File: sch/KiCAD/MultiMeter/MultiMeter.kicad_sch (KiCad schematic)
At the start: 17 parts

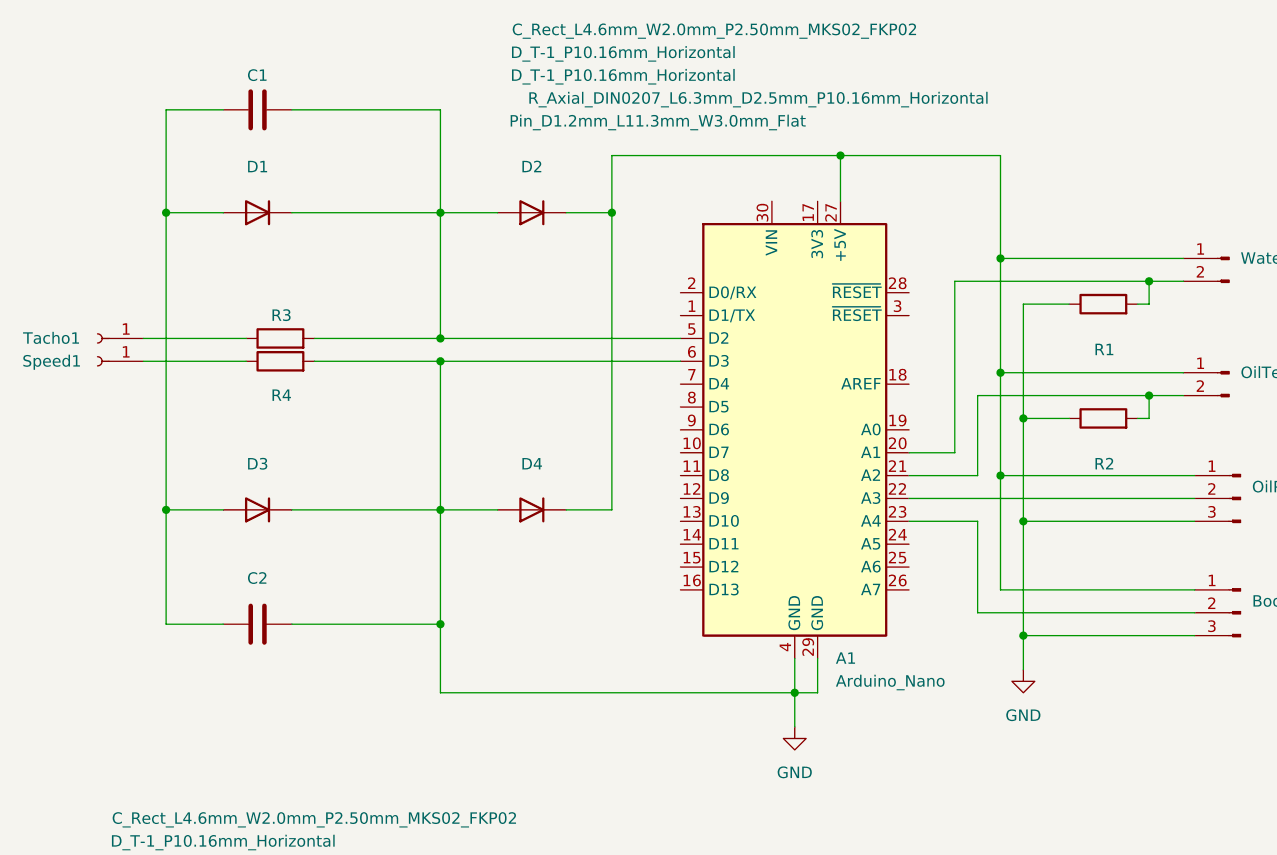
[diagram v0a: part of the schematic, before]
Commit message: 回路図の間違いを修正
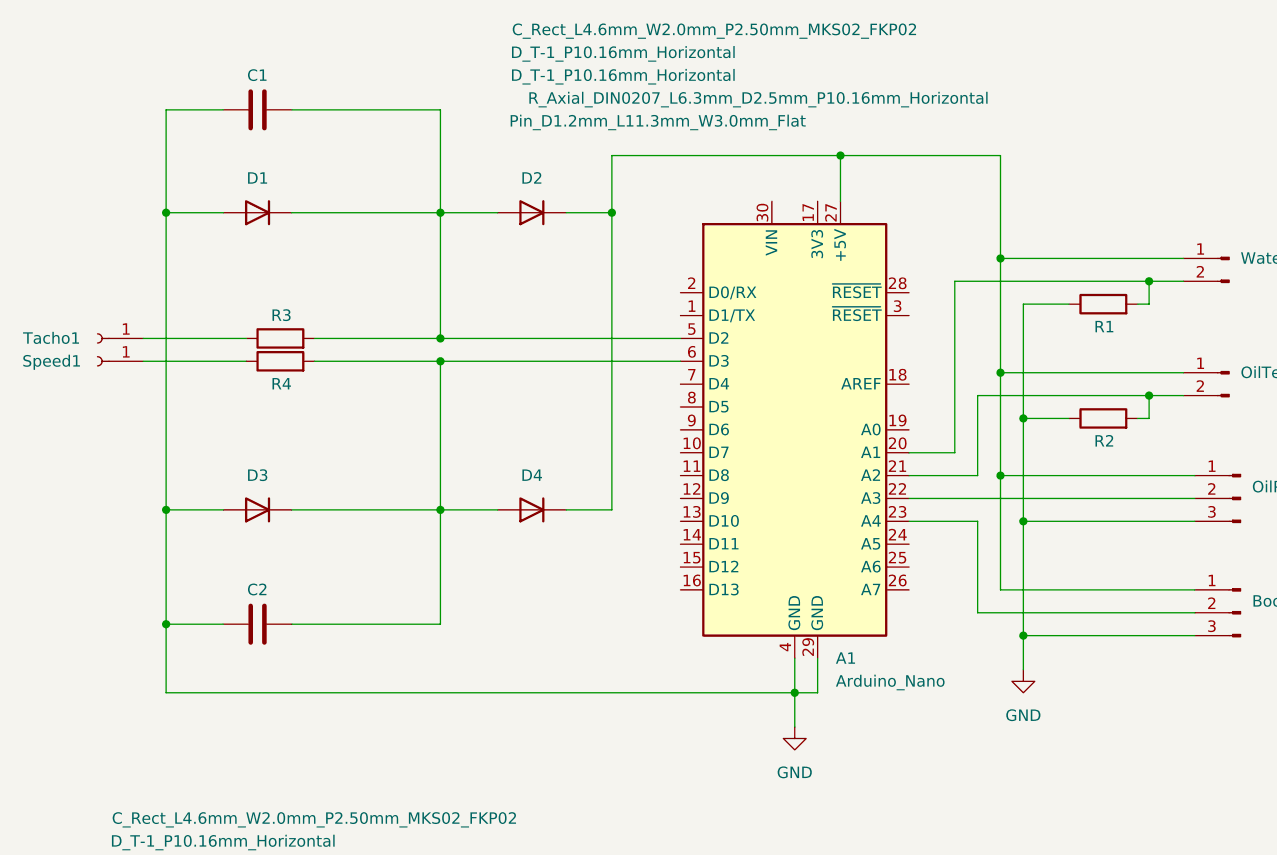
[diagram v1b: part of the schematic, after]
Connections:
- net GND: now also C1.1, C2.1, D1.1 (A), D3.1 (A); no longer A1.6 (D3), C2.2, D3.2 (K), D4.1 (A), R4.2
- new net: A1.6 (D3), C2.2, D3.2 (K), D4.1 (A), R4.2
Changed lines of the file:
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@@
 (kicad_sch (version 20211123) (generator eeschema)
   (paper "A4")
-  (junction (at 62.23 80.01) (diameter 0) (color 0 0 0 0)
-  )
   (junction (at 127 68.58) (diameter 0) (color 0 0 0 0)
   )
@@
   (junction (at 124.46 63.5) (diameter 0) (color 0 0 0 0)
   )
+  (junction (at 31.75 80.01) (diameter 0) (color 0 0 0 0)
+  )
   (junction (at 62.23 34.29) (diameter 0) (color 0 0 0 0)
   )
@@
     (stroke (width 0) (type default) (color 0 0 0 0))
   )
-  (wire (pts (xy 101.6 87.63) (xy 62.23 87.63))
-    (stroke (width 0) (type default) (color 0 0 0 0))
-  )
   (wire (pts (xy 119.38 60.96) (xy 114.3 60.96))
     (stroke (width 0) (type default) (color 0 0 0 0))
@@
     (stroke (width 0) (type default) (color 0 0 0 0))
   )
+  (wire (pts (xy 31.75 87.63) (xy 31.75 80.01))
+    (stroke (width 0) (type default) (color 0 0 0 0))
+  )
   (wire (pts (xy 81.28 34.29) (xy 76.2 34.29))
     (stroke (width 0) (type default) (color 0 0 0 0))
@@
     (stroke (width 0) (type default) (color 0 0 0 0))
   )
-  (wire (pts (xy 62.23 87.63) (xy 62.23 80.01))
-    (stroke (width 0) (type default) (color 0 0 0 0))
-  )
   (wire (pts (xy 144.78 41.91) (xy 140.97 41.91))
     (stroke (width 0) (type default) (color 0 0 0 0))
@@
     (stroke (width 0) (type default) (color 0 0 0 0))
   )
+  (wire (pts (xy 101.6 87.63) (xy 31.75 87.63))
+    (stroke (width 0) (type default) (color 0 0 0 0))
+  )
   (wire (pts (xy 139.7 57.15) (xy 140.97 57.15))
     (stroke (width 0) (type default) (color 0 0 0 0))
@@
   (symbol (lib_id "Device:R") (at 135.89 57.15 90) (unit 1)
     (in_bom yes) (on_board yes)
-    (property "Reference" "R2" (id 0) (at 137.16 62.23 90)
+    (property "Reference" "R2" (id 0) (at 137.16 59.69 90)
       (effects (font (size 1.27 1.27)) (justify left))
     )
@@
   (symbol (lib_id "Simulation_SPICE:DIODE") (at 41.91 67.31 0) (unit 1)
     (in_bom yes) (on_board yes)
-    (property "Reference" "D3" (id 0) (at 41.91 62.23 0))
+    (property "Reference" "D3" (id 0) (at 41.91 63.5 0))
     (property "Value" "D_T-1_P10.16mm_Horizontal" (id 1) (at 38.1 104.14 0))
     (property "Footprint" "Diode_THT:D_T-1_P10.16mm_Horizontal" (id 2) (at 41.91 67.31 0)
@@
   (symbol (lib_id "Device:R") (at 44.45 50.8 90) (unit 1)
     (in_bom yes) (on_board yes)
-    (property "Reference" "R4" (id 0) (at 45.72 54.61 90)
+    (property "Reference" "R4" (id 0) (at 45.72 53.34 90)
       (effects (font (size 1.27 1.27)) (justify left))
     )
@@
   (symbol (lib_id "Device:C") (at 41.91 80.01 90) (unit 1)
     (in_bom yes) (on_board yes)
-    (property "Reference" "C2" (id 0) (at 41.91 74.93 90))
+    (property "Reference" "C2" (id 0) (at 41.91 76.2 90))
     (property "Value" "C_Rect_L4.6mm_W2.0mm_P2.50mm_MKS02_FKP02" (id 1) (at 48.26 101.6 90))
     (property "Footprint" "Capacitor_THT:C_Rect_L4.6mm_W2.0mm_P2.50mm_MKS02_FKP02" (id 2) (at 45.72 79.0448 0)
@@
   (symbol (lib_id "Simulation_SPICE:DIODE") (at 72.39 34.29 0) (unit 1)
     (in_bom yes) (on_board yes)
-    (property "Reference" "D2" (id 0) (at 72.39 29.21 0))
+    (property "Reference" "D2" (id 0) (at 72.39 30.48 0))
     (property "Value" "D_T-1_P10.16mm_Horizontal" (id 1) (at 82.55 19.05 0))
     (property "Footprint" "Diode_THT:D_T-1_P10.16mm_Horizontal" (id 2) (at 72.39 34.29 0)
@@
   (symbol (lib_id "Simulation_SPICE:DIODE") (at 41.91 34.29 0) (unit 1)
     (in_bom yes) (on_board yes)
-    (property "Reference" "D1" (id 0) (at 41.91 29.21 0))
+    (property "Reference" "D1" (id 0) (at 41.91 30.48 0))
     (property "Value" "D_T-1_P10.16mm_Horizontal" (id 1) (at 82.55 16.51 0))
     (property "Footprint" "Diode_THT:D_T-1_P10.16mm_Horizontal" (id 2) (at 41.91 34.29 0)
@@
   (symbol (lib_id "Simulation_SPICE:DIODE") (at 72.39 67.31 0) (unit 1)
     (in_bom yes) (on_board yes)
-    (property "Reference" "D4" (id 0) (at 72.39 62.23 0))
+    (property "Reference" "D4" (id 0) (at 72.39 63.5 0))
     (property "Value" "D_T-1_P10.16mm_Horizontal" (id 1) (at 38.1 106.68 0))
     (property "Footprint" "Diode_THT:D_T-1_P10.16mm_Horizontal" (id 2) (at 72.39 67.31 0)
@@
   (symbol (lib_id "Device:R") (at 135.89 44.45 90) (unit 1)
     (in_bom yes) (on_board yes)
-    (property "Reference" "R1" (id 0) (at 137.16 49.53 90)
-      (effects (font (size 1.27 1.27)) (justify left))
-    )
+    (property "Reference" "R1" (id 0) (at 137.16 46.99 90)
+      (effects (font (size 1.27 1.27)) (justify left))
+    )

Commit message: 回路図データ修正
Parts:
- removed Boost, OilPress: PinHeader_1x03_P2.54mm_Vertical, Connector_PinHeader_2.54mm:PinHeader_1x03_P2.54mm_Vertical, symbol Connector:Conn_01x03_Male
- removed C1, C2: C_Rect_L4.6mm_W2.0mm_P2.50mm_MKS02_FKP02, Capacitor_THT:C_Rect_L4.6mm_W2.0mm_P2.50mm_MKS02_FKP02, symbol Device:C
- removed D1, D2, D3, D4: D_T-1_P10.16mm_Horizontal, Diode_THT:D_T-1_P10.16mm_Horizontal, symbol Simulation_SPICE:DIODE
- removed OilTemp, WaterTemp: PinHeader_1x02_P2.54mm_Vertical, Connector_PinHeader_2.54mm:PinHeader_1x02_P2.54mm_Vertical, symbol Connector:Conn_01x02_Male
- removed Speed1, Tacho1: Pin_D1.2mm_L11.3mm_W3.0mm_Flat, Connector_Pin:Pin_D1.2mm_L11.3mm_W3.0mm_Flat, symbol Connector:Conn_01x01_Female
- added C1, C2: (no value), symbol pspice:C
- added D1, D2, D3, D4: 1N4148, Diode_THT:D_DO-35_SOD27_P7.62mm_Horizontal, symbol Diode:1N4148
- added J1, J2: (no value), symbol Connector:Conn_01x02_Male
- added J3, J4: (no value), symbol Connector:Conn_01x03_Male
- added J5: (no value), symbol Connector:Conn_01x02_Female
- A1: value Arduino_Nano -> Arduino_Nano_v3.x
- R1, R2, R3, R4: value R_Axial_DIN0207_L6.3mm_D2.5mm_P10.16mm_Horizontal -> (none); footprint Resistor_THT:R_Axial_DIN0207_L6.3mm_D2.5mm_P10.16mm_Horizontal -> (none)
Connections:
- net at A1.21 (A2): now also R2.1, J2.2 (Pin_2); no longer R2.2
- net at A1.6 (D3): now also R4.1, C2.1, D3.1 (K), D4.2 (A); no longer R4.2
- net at A1.27 (+5V): now also D2.1 (K), D4.1 (K), J1.1 (Pin_1), J2.1 (Pin_1), J3.1 (Pin_1), J4.1 (Pin_1)
- net at A1.22 (A3): now also J3.2 (Pin_2)
- net at A1.5 (D2): now also R3.1, C1.1, D1.1 (K), D2.2 (A); no longer R3.2
- net at R1.2: now also A1.29 (GND), A1.4 (GND), R2.2, C1.2, C2.2, D1.2 (A), D3.2 (A), J3.3 (Pin_3), J4.3 (Pin_3); no longer A1.20 (A1)
- net at A1.23 (A4): now also J4.2 (Pin_2)
- removed net GND: A1.29 (GND), A1.4 (GND), R1.1, R2.1
- new net: J5.2 (Pin_2), R4.2
- new net: J5.1 (Pin_1), R3.2
- new net: A1.20 (A1), J1.2 (Pin_2), R1.1

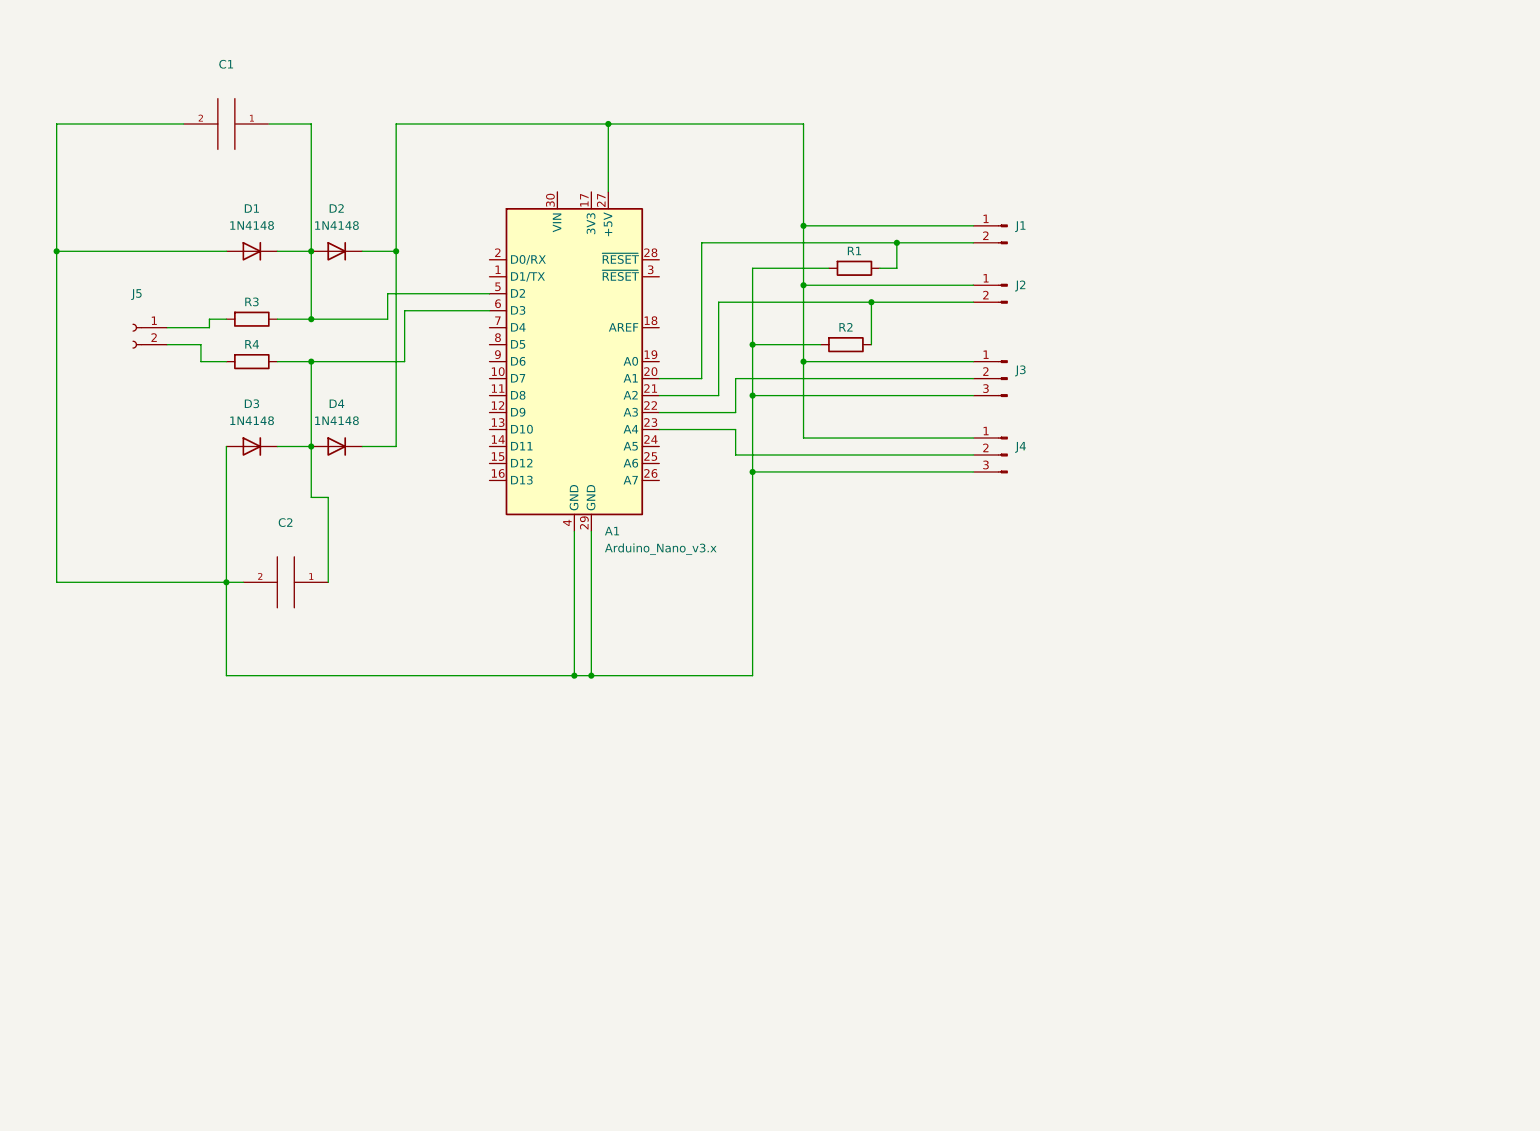
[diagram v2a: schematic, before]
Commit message: デバック用PADを追加
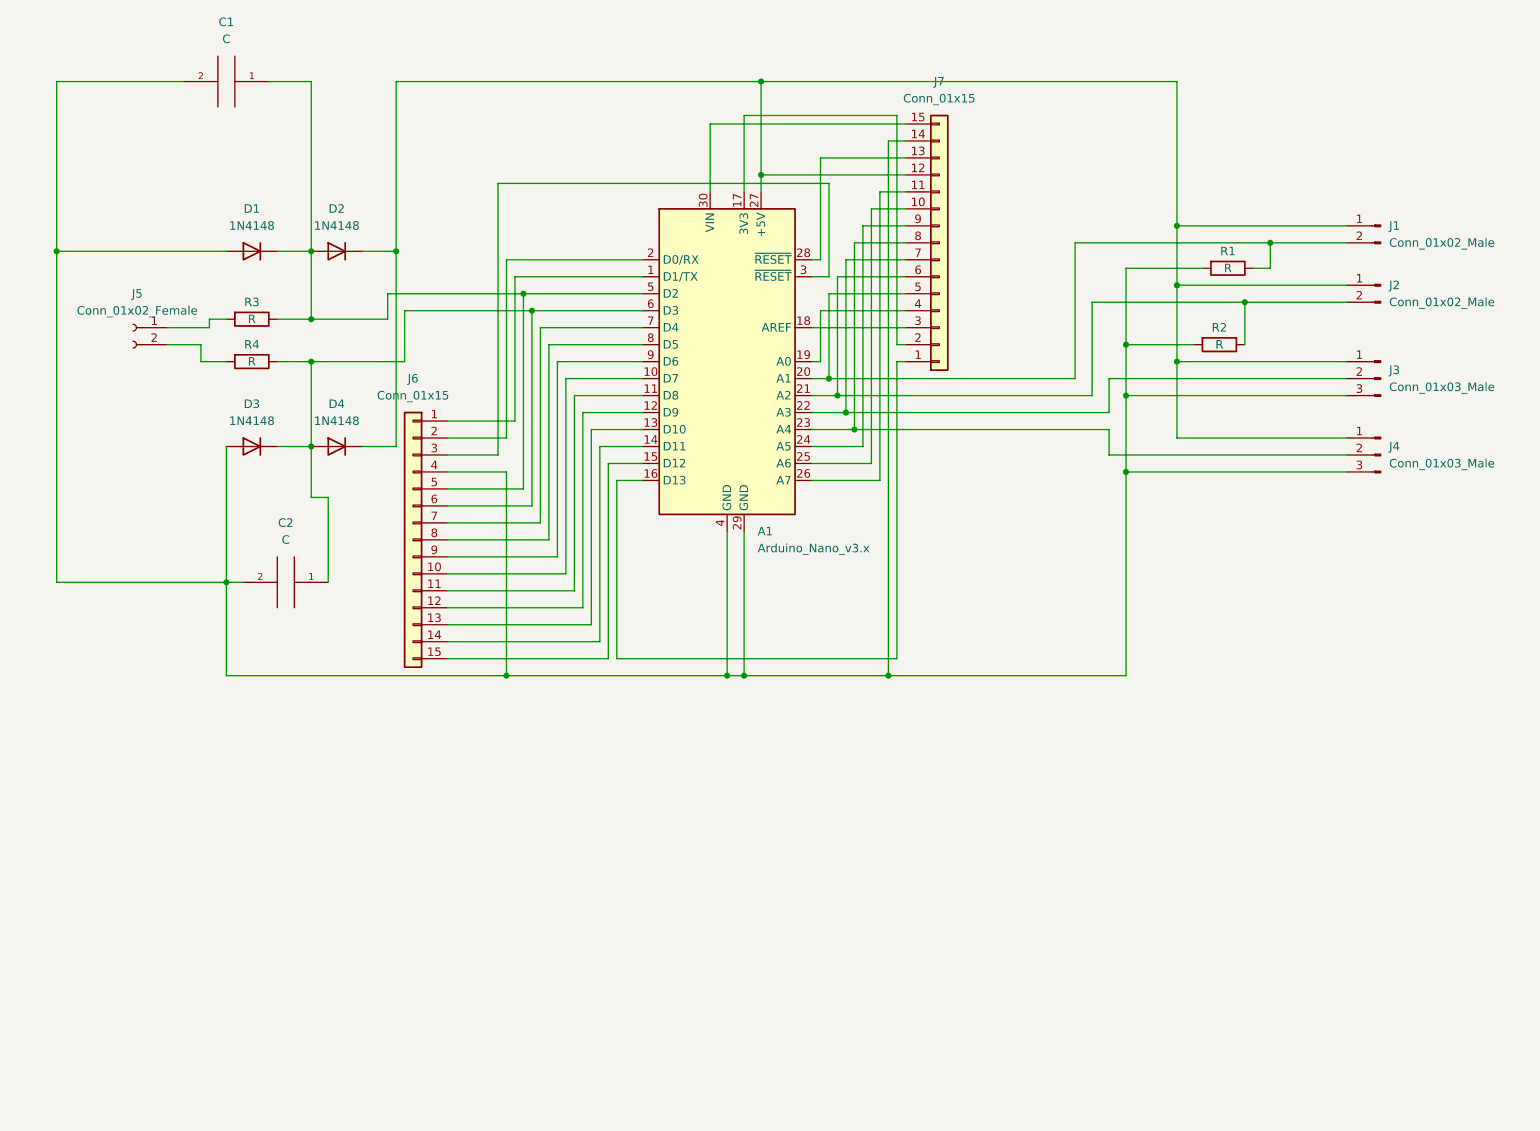
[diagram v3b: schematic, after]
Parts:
- added J6, J7: Conn_01x15, Connector_PinSocket_2.54mm:PinSocket_1x15_P2.54mm_Vertical, symbol Connector_Generic:Conn_01x15
- C1, C2: value (none) -> C; footprint (none) -> Capacitor_THT:C_Rect_L4.6mm_W2.0mm_P2.50mm_MKS02_FKP02
- J1, J2: value (none) -> Conn_01x02_Male; footprint (none) -> Connector_Molex:Molex_SPOX_5267-02A_1x02_P2.50mm_Vertical
- J3, J4: value (none) -> Conn_01x03_Male; footprint (none) -> Connector_Molex:Molex_SPOX_5267-03A_1x03_P2.50mm_Vertical
- J5: value (none) -> Conn_01x02_Female; footprint (none) -> Connector_Molex:Molex_KK-254_AE-6410-02A_1x02_P2.54mm_Vertical
- R1, R2, R3, R4: value (none) -> R; footprint (none) -> Resistor_THT:R_Axial_DIN0204_L3.6mm_D1.6mm_P7.62mm_Horizontal
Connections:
- net at A1.6 (D3), C2.1, D3.1 (K)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: now also J6.6 (Pin_6)
- net at A1.27 (+5V), D2.1 (K), D4.1 (K)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: now also J7.12 (Pin_12)
- net at A1.21 (A2), J2.2 (Pin_2), R2.1: now also J7.6 (Pin_6)
- net at A1.5 (D2), C1.1, D1.1 (K)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: now also J6.5 (Pin_5)
- net at A1.29 (GND), A1.4 (GND), C1.2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: now also J6.4 (Pin_4), J7.14 (Pin_14)
- net at A1.22 (A3), J3.2 (Pin_2): now also J7.7 (Pin_7)
- net at A1.23 (A4), J4.2 (Pin_2): now also J7.8 (Pin_8)
- net at A1.20 (A1), J1.2 (Pin_2), R1.1: now also J7.5 (Pin_5)
- net at A1.1 (D1/TX): now also J6.1 (Pin_1)
- net at A1.10 (D7): now also J6.10 (Pin_10)
- net at A1.11 (D8): now also J6.11 (Pin_11)
- net at A1.12 (D9): now also J6.12 (Pin_12)
- net at A1.13 (D10): now also J6.13 (Pin_13)
- net at A1.14 (D11): now also J6.14 (Pin_14)
- net at A1.15 (D12): now also J6.15 (Pin_15)
- net at A1.16 (D13): now also J7.1 (Pin_1)
- net at A1.17 (3V3): now also J7.2 (Pin_2)
- net at A1.18 (AREF): now also J7.3 (Pin_3)
- net at A1.19 (A0): now also J7.4 (Pin_4)
- net at A1.2 (D0/RX): now also J6.2 (Pin_2)
- net at A1.24 (A5): now also J7.9 (Pin_9)
- net at A1.25 (A6): now also J7.10 (Pin_10)
- net at A1.26 (A7): now also J7.11 (Pin_11)
- net at A1.28 (~{RESET}): now also J7.13 (Pin_13)
- net at A1.3 (~{RESET}): now also J6.3 (Pin_3)
- net at A1.30 (VIN): now also J7.15 (Pin_15)
- net at A1.7 (D4): now also J6.7 (Pin_7)
- net at A1.8 (D5): now also J6.8 (Pin_8)
- net at A1.9 (D6): now also J6.9 (Pin_9)
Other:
- moved on the sheet: A1, C1, J1, J2, J3, J4, R1, R2
